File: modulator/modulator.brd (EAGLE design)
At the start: 100 x 40 mm, 43 parts, among them IC1 LM741P, T2 BF173

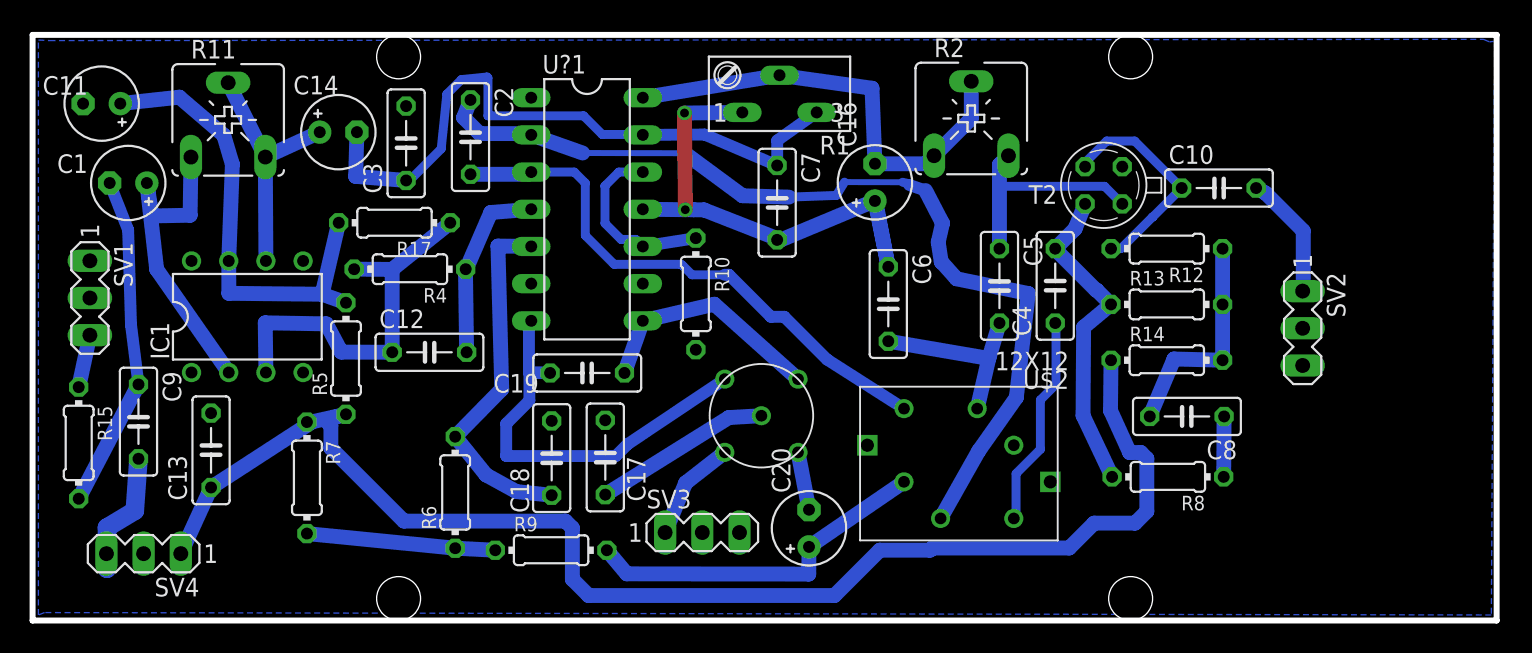
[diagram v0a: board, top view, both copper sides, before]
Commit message: rearrange the elements on the PCB.
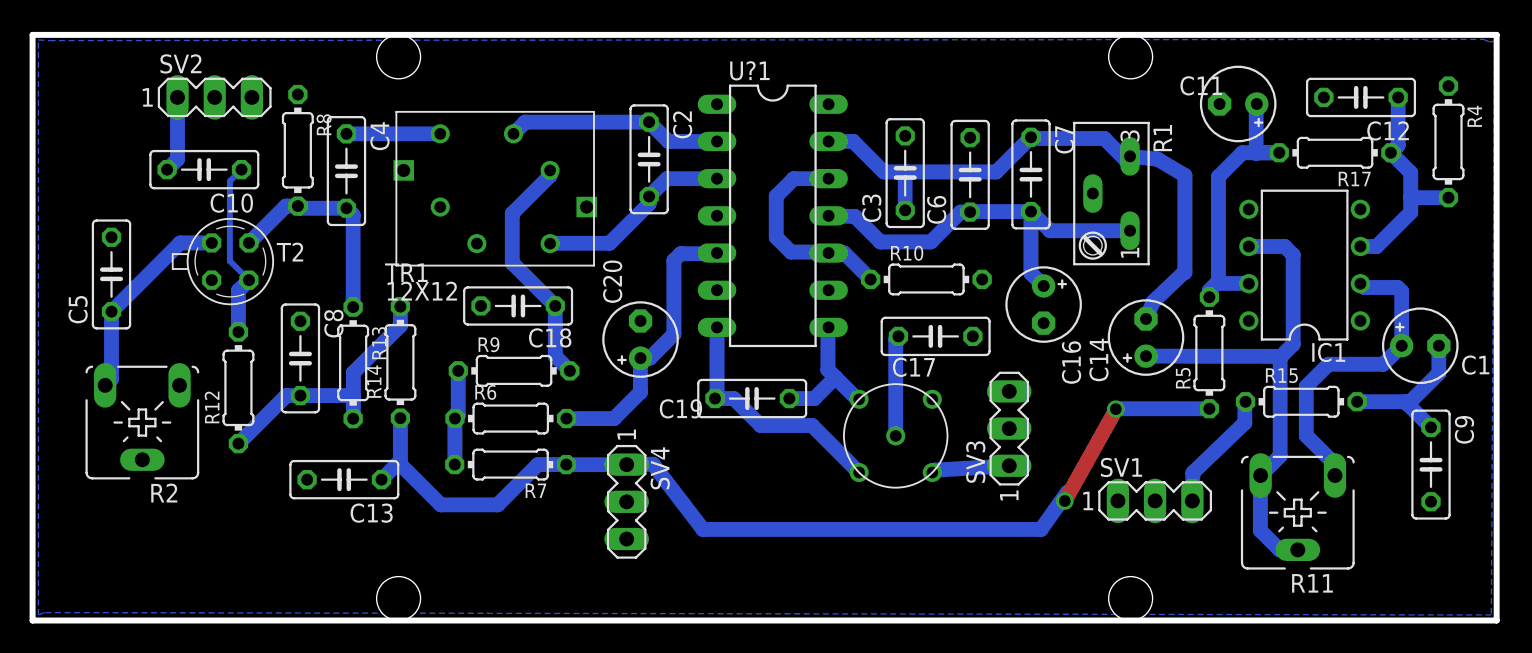
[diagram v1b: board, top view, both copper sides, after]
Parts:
- removed U$2: 12X12, sp5ww:12X12
- removed U$3: TR5X5, sp5ww:TR5X5
- added TR1: 12X12, sp5ww:12X12
- added TR2: TR5X5, sp5ww:TR5X5
- moved C1 88.9 mm to (94.8, 18.8), turned to 0 degrees
- moved C9 88.3 mm to (95.5, 10.7)
- moved R15 83.6 mm to (86.7, 14.9), turned to 0 degrees
- moved R11 77.8 mm to (86.4, 7.36), turned to 180 degrees
- moved C11 77.6 mm to (82.3, 35.3)
- moved SV2 76.0 mm to (12.4, 35.7), turned to 0 degrees
- moved SV1 74.1 mm to (76.7, 8.17), turned to 0 degrees
- moved IC1 72.3 mm to (86.9, 24.3), turned to 90 degrees
- moved R4 71.5 mm to (96.7, 32.7), turned to 270 degrees
- moved C10 69.3 mm to (11.7, 30.8), turned to 180 degrees
- moved C12 66.0 mm to (90.7, 35.7), turned to 180 degrees
- moved R17 64.4 mm to (89.0, 31.9)
- moved R12 64.1 mm to (14.1, 15.9), turned to 90 degrees
- moved R8 63.5 mm to (18.1, 32.1), turned to 270 degrees
- moved C8 60.7 mm to (18.3, 17.9), turned to 270 degrees
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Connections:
- net GND: now also TR1.D, TR1.GND1, TR1.GND2, TR2.P$4; no longer U$2.D, U$2.GND1, U$2.GND2, U$3.P$4
- net N$10: now also TR1.C; no longer U$2.C
- net N$11: now also C20.+; no longer C18.2
- net N$12: now also TR2.P$2; no longer U$3.P$2
- net N$15: now also TR2.P$3; no longer U$3.P$3
- net N$16: now also TR2.P$1; no longer U$3.P$1
- net N$21: now also C18.2, TR1.B; no longer C20.+, U$2.B
- net N$22: now also TR2.P$5; no longer U$3.P$5
- net N$25: now also TR1.G; no longer U$2.G
- net N$9: now also TR1.A; no longer U$2.A
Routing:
- net GND: track 74.8 -> 0.00 mm
- net N$9: track 63.8 -> 14.8 mm
- net +12V: track 95.4 -> 70.5 mm, vias 0 -> 2
- net N$10: track 38.1 -> 13.5 mm
- net N$6: track 16.9 -> 35.3 mm
- net N$16: track 29.5 -> 16.9 mm
- net N$3: track 22.8 -> 10.6 mm
- net N$4: track 32.1 -> 20.5 mm
- net N$2: track 26.6 -> 15.6 mm
- net N$8: track 36.7 -> 28.2 mm, vias 2 -> 0
- net N$25: track 14.6 -> 6.41 mm
- net N$21: track 24.3 -> 16.4 mm
- net N$13: track 22.3 -> 14.7 mm
- net N$15: track 16.5 -> 9.63 mm
- net N$19: track 12.9 -> 6.50 mm
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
